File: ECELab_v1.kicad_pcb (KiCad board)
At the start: 4 copper layers, 147.5 x 89.3 mm, 131 parts, among them J201 USB_C_Receptacle_USB2.0, J202 Conn_01x06_Male, J301 Conn_01x04_Male, J302 Conn_01x03_Male, J303 Conn_01x03_Male, J401 USB_C_Receptacle_USB2.0, J402 Conn_01x02_Male, J501 Conn_02x20_Odd_Even, J502 Conn_02x20_Odd_Even, J503 Conn_02x20_Odd_Even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

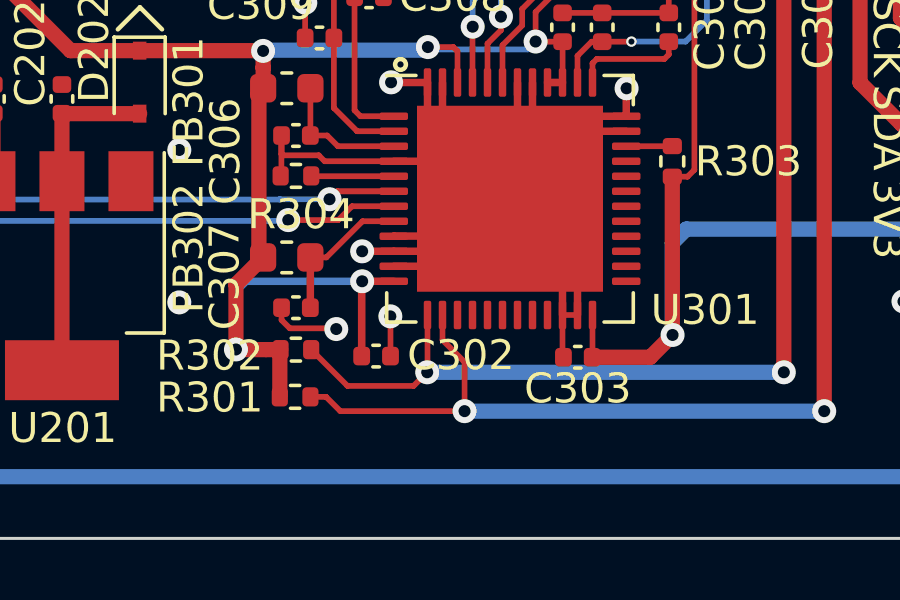
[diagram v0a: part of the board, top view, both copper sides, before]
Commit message: Fix FTDI 1 Channel SDA issue
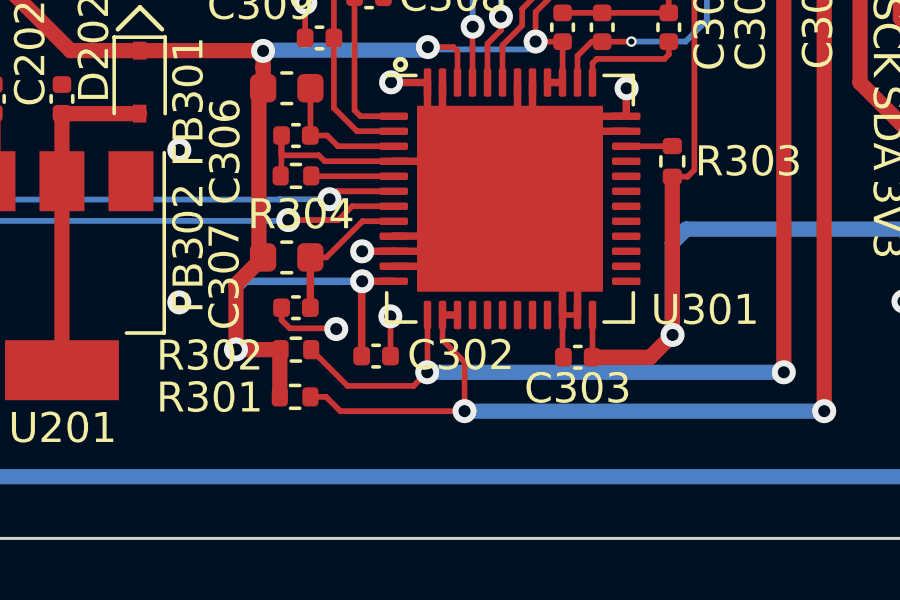
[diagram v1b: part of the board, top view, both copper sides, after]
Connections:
- net IO.LEFT0 renamed /GPIO Expansion/IO.LEFT0
- net IO.LEFT1 renamed /GPIO Expansion/IO.LEFT1
- net IO.LEFT2 renamed /GPIO Expansion/IO.LEFT2
- net IO.LEFT3 renamed /GPIO Expansion/IO.LEFT3
- net IO.LEFT4 renamed /GPIO Expansion/IO.LEFT4
- net IO.LEFT5 renamed /GPIO Expansion/IO.LEFT5
- net IO.LEFT6 renamed /GPIO Expansion/IO.LEFT6
- net IO.LEFT7 renamed /GPIO Expansion/IO.LEFT7
- net IO.PB0 renamed /GPIO Expansion/IO.PB0
- net IO.PB1 renamed /GPIO Expansion/IO.PB1
- net IO.PB10 renamed /GPIO Expansion/IO.PB10
- net IO.PB11 renamed /GPIO Expansion/IO.PB11
- net IO.PB12 renamed /GPIO Expansion/IO.PB12
- net IO.PB13 renamed /GPIO Expansion/IO.PB13
- net IO.PB14 renamed /GPIO Expansion/IO.PB14
- net IO.PB15 renamed /GPIO Expansion/IO.PB15
- net IO.PB16 renamed /GPIO Expansion/IO.PB16
- net IO.PB17 renamed /GPIO Expansion/IO.PB17
- net IO.PB18 renamed /GPIO Expansion/IO.PB18
- net IO.PB19 renamed /GPIO Expansion/IO.PB19
- net IO.PB2 renamed /GPIO Expansion/IO.PB2
- net IO.PB3 renamed /GPIO Expansion/IO.PB3
- net IO.PB4 renamed /GPIO Expansion/IO.PB4
- net IO.PB5 renamed /GPIO Expansion/IO.PB5
- net IO.PB6 renamed /GPIO Expansion/IO.PB6
- net IO.PB7 renamed /GPIO Expansion/IO.PB7
- net IO.PB8 renamed /GPIO Expansion/IO.PB8
- net IO.PB9 renamed /GPIO Expansion/IO.PB9
- net IO.RIGHT0 renamed /GPIO Expansion/IO.RIGHT0
- net IO.RIGHT1 renamed /GPIO Expansion/IO.RIGHT1
- net IO.RIGHT2 renamed /GPIO Expansion/IO.RIGHT2
- net IO.RIGHT3 renamed /GPIO Expansion/IO.RIGHT3
- net IO.RIGHT4 renamed /GPIO Expansion/IO.RIGHT4
- net IO.RIGHT5 renamed /GPIO Expansion/IO.RIGHT5
- net IO.RIGHT6 renamed /GPIO Expansion/IO.RIGHT6
- net IO.RIGHT7 renamed /GPIO Expansion/IO.RIGHT7
- U301 pad 15: unconnected-(U301-Pad15) -> FTDI.SDA
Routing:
- net FTDI.SDA: track 83.1 -> 83.6 mm

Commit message: Complete V1.3
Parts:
- U411: value NE555DR -> LMC555CMX/NOPB
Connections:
- net /GPIO Expansion/IO.LEFT0 renamed IO.LEFT0
- net /GPIO Expansion/IO.LEFT1 renamed IO.LEFT1
- net /GPIO Expansion/IO.LEFT2 renamed IO.LEFT2
- net /GPIO Expansion/IO.LEFT3 renamed IO.LEFT3
- net /GPIO Expansion/IO.LEFT4 renamed IO.LEFT4
- net /GPIO Expansion/IO.LEFT5 renamed IO.LEFT5
- net /GPIO Expansion/IO.LEFT6 renamed IO.LEFT6
- net /GPIO Expansion/IO.LEFT7 renamed IO.LEFT7
- net /GPIO Expansion/IO.PB0 renamed IO.PB0
- net /GPIO Expansion/IO.PB1 renamed IO.PB1
- net /GPIO Expansion/IO.PB10 renamed IO.PB10
- net /GPIO Expansion/IO.PB11 renamed IO.PB11
- net /GPIO Expansion/IO.PB12 renamed IO.PB12
- net /GPIO Expansion/IO.PB13 renamed IO.PB13
- net /GPIO Expansion/IO.PB14 renamed IO.PB14
- net /GPIO Expansion/IO.PB15 renamed IO.PB15
- net /GPIO Expansion/IO.PB16 renamed IO.PB16
- net /GPIO Expansion/IO.PB17 renamed IO.PB17
- net /GPIO Expansion/IO.PB18 renamed IO.PB18
- net /GPIO Expansion/IO.PB19 renamed IO.PB19
- net /GPIO Expansion/IO.PB2 renamed IO.PB2
- net /GPIO Expansion/IO.PB3 renamed IO.PB3
- net /GPIO Expansion/IO.PB4 renamed IO.PB4
- net /GPIO Expansion/IO.PB5 renamed IO.PB5
- net /GPIO Expansion/IO.PB6 renamed IO.PB6
- net /GPIO Expansion/IO.PB7 renamed IO.PB7
- net /GPIO Expansion/IO.PB8 renamed IO.PB8
- net /GPIO Expansion/IO.PB9 renamed IO.PB9
- net /GPIO Expansion/IO.RIGHT0 renamed IO.RIGHT0
- net /GPIO Expansion/IO.RIGHT1 renamed IO.RIGHT1
- net /GPIO Expansion/IO.RIGHT2 renamed IO.RIGHT2
- net /GPIO Expansion/IO.RIGHT3 renamed IO.RIGHT3
- net /GPIO Expansion/IO.RIGHT4 renamed IO.RIGHT4
- net /GPIO Expansion/IO.RIGHT5 renamed IO.RIGHT5
- net /GPIO Expansion/IO.RIGHT6 renamed IO.RIGHT6
- net /GPIO Expansion/IO.RIGHT7 renamed IO.RIGHT7
- net /GPIO Expansion/IO.SS0_0 renamed IO.SS0_0
- net /GPIO Expansion/IO.SS0_1 renamed IO.SS0_1
- net /GPIO Expansion/IO.SS0_2 renamed IO.SS0_2
- net /GPIO Expansion/IO.SS0_3 renamed IO.SS0_3
- net /GPIO Expansion/IO.SS0_4 renamed IO.SS0_4
- net /GPIO Expansion/IO.SS0_5 renamed IO.SS0_5
- net /GPIO Expansion/IO.SS0_6 renamed IO.SS0_6
- net /GPIO Expansion/IO.SS0_7 renamed IO.SS0_7
- net /GPIO Expansion/IO.SS1_0 renamed IO.SS1_0
- net /GPIO Expansion/IO.SS1_1 renamed IO.SS1_1
- net /GPIO Expansion/IO.SS1_2 renamed IO.SS1_2
- net /GPIO Expansion/IO.SS1_3 renamed IO.SS1_3
- net /GPIO Expansion/IO.SS1_4 renamed IO.SS1_4
- net /GPIO Expansion/IO.SS1_5 renamed IO.SS1_5
- net /GPIO Expansion/IO.SS1_6 renamed IO.SS1_6
- net /GPIO Expansion/IO.SS1_7 renamed IO.SS1_7
- net /GPIO Expansion/IO.SS2_0 renamed IO.SS2_0
- net /GPIO Expansion/IO.SS2_1 renamed IO.SS2_1
- net /GPIO Expansion/IO.SS2_2 renamed IO.SS2_2
- net /GPIO Expansion/IO.SS2_3 renamed IO.SS2_3
- net /GPIO Expansion/IO.SS2_4 renamed IO.SS2_4
- net /GPIO Expansion/IO.SS2_5 renamed IO.SS2_5
- net /GPIO Expansion/IO.SS2_6 renamed IO.SS2_6
- net /GPIO Expansion/IO.SS2_7 renamed IO.SS2_7
- net /GPIO Expansion/IO.SS3_0 renamed IO.SS3_0
- net /GPIO Expansion/IO.SS3_1 renamed IO.SS3_1
- net /GPIO Expansion/IO.SS3_2 renamed IO.SS3_2
- net /GPIO Expansion/IO.SS3_3 renamed IO.SS3_3
- net /GPIO Expansion/IO.SS3_4 renamed IO.SS3_4
- net /GPIO Expansion/IO.SS3_5 renamed IO.SS3_5
- net /GPIO Expansion/IO.SS3_6 renamed IO.SS3_6
- net /GPIO Expansion/IO.SS3_7 renamed IO.SS3_7
- net IO.SS4_0 renamed /GPIO Expansion/IO.SS4_0
- net IO.SS4_1 renamed /GPIO Expansion/IO.SS4_1
- net IO.SS4_2 renamed /GPIO Expansion/IO.SS4_2
- net IO.SS4_3 renamed /GPIO Expansion/IO.SS4_3
- net IO.SS4_4 renamed /GPIO Expansion/IO.SS4_4
- net IO.SS4_5 renamed /GPIO Expansion/IO.SS4_5
- net IO.SS4_6 renamed /GPIO Expansion/IO.SS4_6
- net IO.SS4_7 renamed /GPIO Expansion/IO.SS4_7
- net IO.SS5_0 renamed /GPIO Expansion/IO.SS5_0
- net IO.SS5_1 renamed /GPIO Expansion/IO.SS5_1
- net IO.SS5_2 renamed /GPIO Expansion/IO.SS5_2
- net IO.SS5_3 renamed /GPIO Expansion/IO.SS5_3
- net IO.SS5_4 renamed /GPIO Expansion/IO.SS5_4
- net IO.SS5_5 renamed /GPIO Expansion/IO.SS5_5
- net IO.SS5_6 renamed /GPIO Expansion/IO.SS5_6
- net IO.SS5_7 renamed /GPIO Expansion/IO.SS5_7
- net IO.SS6_0 renamed /GPIO Expansion/IO.SS6_0
- net IO.SS6_1 renamed /GPIO Expansion/IO.SS6_1
- net IO.SS6_2 renamed /GPIO Expansion/IO.SS6_2
- net IO.SS6_3 renamed /GPIO Expansion/IO.SS6_3
- net IO.SS6_4 renamed /GPIO Expansion/IO.SS6_4
- net IO.SS6_5 renamed /GPIO Expansion/IO.SS6_5
- net IO.SS6_6 renamed /GPIO Expansion/IO.SS6_6
- net IO.SS6_7 renamed /GPIO Expansion/IO.SS6_7
- net IO.SS7_0 renamed /GPIO Expansion/IO.SS7_0
- net IO.SS7_1 renamed /GPIO Expansion/IO.SS7_1
- net IO.SS7_2 renamed /GPIO Expansion/IO.SS7_2
- net IO.SS7_3 renamed /GPIO Expansion/IO.SS7_3
- net IO.SS7_4 renamed /GPIO Expansion/IO.SS7_4
- net IO.SS7_5 renamed /GPIO Expansion/IO.SS7_5
- net IO.SS7_6 renamed /GPIO Expansion/IO.SS7_6
- net IO.SS7_7 renamed /GPIO Expansion/IO.SS7_7
- R417 pad 1: +5V -> +3V3
- U411 pad 4: +5V -> +3V3
- U411 pad 8: +5V -> +3V3
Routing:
- net +5V: track 197.1 -> 160.1 mm, vias 7 -> 5
- net +3V3: track 758.2 -> 788.6 mm, vias 37 -> 39
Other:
- board text added: "CLK100"
- board text added: "ECELabs PCB Design v1.3 Minh Nguyen Junfei Li"
- board text added: "GPIO"
- board text added: "I2C"
- board text added: "PB20"
- board text added: "Pi4B USB THIS DIRECTION"
